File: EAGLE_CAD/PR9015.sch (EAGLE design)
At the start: 73 parts, among them J1 M3_SCREW_POST, SW1 C&K_PTS645

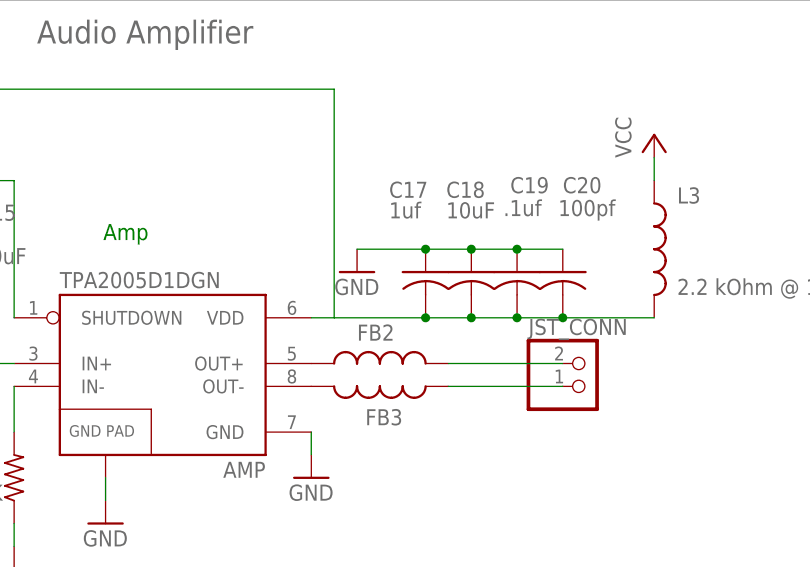
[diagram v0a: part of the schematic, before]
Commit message: okay, now we're good i think
copied R_US over to PR_Parts_Library. Then added a new package variant
and connected it with my c0402 package (created from Chris’s email).
Then went into the .brd and replaced C17 with my new part. Seems to
work.
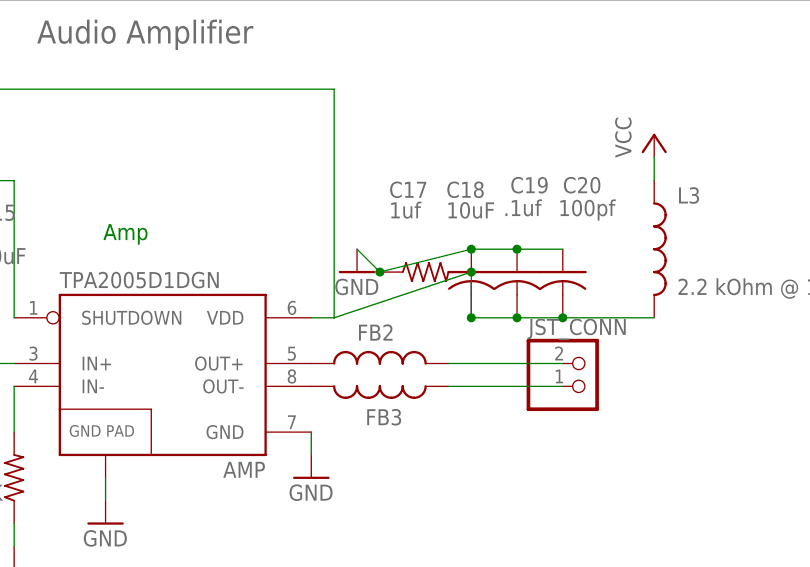
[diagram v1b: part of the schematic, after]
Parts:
- C17: device resistor:C-USC0402 -> PR_Parts_Library:R-US_
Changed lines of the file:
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@@
 <?xml version="1.0" encoding="utf-8"?>
 <!DOCTYPE eagle SYSTEM "eagle.dtd">
-<eagle version="7.2.0">
+<eagle version="6.6.0">
 <drawing>
 <settings>
@@
 <part name="C14" library="resistor" deviceset="C-US" device="C0603" value="10uF"/>
 <part name="C15" library="resistor" deviceset="C-US" device="C0603" value="10uF"/>
-<part name="C17" library="resistor" deviceset="C-US" device="C0402" value="1uf"/>
+<part name="C17" library="PR_Parts_Library" deviceset="R-US_" device="" value="1uf"/>
 <part name="C9" library="resistor" deviceset="C-US" device="C0402" value="1uF"/>
 <part name="FET2" library="PR_Parts_Library" deviceset="AO3435" device=""/>
@@
 <pinref part="C18" gate="G$1" pin="1"/>
 <junction x="208.28" y="53.34"/>
-<wire x1="208.28" y1="53.34" x2="203.2" y2="53.34" width="0.1524" layer="91"/>
+<wire x1="208.28" y1="53.34" x2="198.12" y2="50.8" width="0.1524" layer="91"/>
 <pinref part="C17" gate="G$1" pin="1"/>
-<wire x1="203.2" y1="53.34" x2="195.58" y2="53.34" width="0.1524" layer="91"/>
-<junction x="203.2" y="53.34"/>
+<wire x1="198.12" y1="50.8" x2="195.58" y2="53.34" width="0.1524" layer="91"/>
+<junction x="198.12" y="50.8"/>
 </segment>
 <segment>
@@
 <wire x1="190.5" y1="45.72" x2="193.04" y2="45.72" width="0.1524" layer="91"/>
 <pinref part="L3" gate="G$1" pin="2"/>
-<wire x1="193.04" y1="45.72" x2="203.2" y2="45.72" width="0.1524" layer="91"/>
-<wire x1="203.2" y1="45.72" x2="208.28" y2="45.72" width="0.1524" layer="91"/>
+<wire x1="193.04" y1="45.72" x2="208.28" y2="50.8" width="0.1524" layer="91"/>
+<wire x1="208.28" y1="50.8" x2="208.28" y2="45.72" width="0.1524" layer="91"/>
 <wire x1="208.28" y1="45.72" x2="213.36" y2="45.72" width="0.1524" layer="91"/>
 <wire x1="213.36" y1="45.72" x2="218.44" y2="45.72" width="0.1524" layer="91"/>
@@
 <junction x="208.28" y="45.72"/>
 <pinref part="C17" gate="G$1" pin="2"/>
-<junction x="203.2" y="45.72"/>
-</segment>
-</net>
+<junction x="208.28" y="50.8"/>
+</segment>
+</net>

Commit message: Revert cea9e40..4e97d22
This rolls back to commit cea9e40d509ff5bb8dd7e4369702d55ec1f1bc0f.
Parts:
- C17: device PR_Parts_Library:R-US_ -> resistor:C-USC0402
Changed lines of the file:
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@@
 <?xml version="1.0" encoding="utf-8"?>
 <!DOCTYPE eagle SYSTEM "eagle.dtd">
-<eagle version="6.6.0">
+<eagle version="7.2.0">
 <drawing>
 <settings>
@@
 <part name="C14" library="resistor" deviceset="C-US" device="C0603" value="10uF"/>
 <part name="C15" library="resistor" deviceset="C-US" device="C0603" value="10uF"/>
-<part name="C17" library="PR_Parts_Library" deviceset="R-US_" device="" value="1uf"/>
+<part name="C17" library="resistor" deviceset="C-US" device="C0402" value="1uf"/>
 <part name="C9" library="resistor" deviceset="C-US" device="C0402" value="1uF"/>
 <part name="FET2" library="PR_Parts_Library" deviceset="AO3435" device=""/>
@@
 <pinref part="C18" gate="G$1" pin="1"/>
 <junction x="208.28" y="53.34"/>
-<wire x1="208.28" y1="53.34" x2="198.12" y2="50.8" width="0.1524" layer="91"/>
+<wire x1="208.28" y1="53.34" x2="203.2" y2="53.34" width="0.1524" layer="91"/>
 <pinref part="C17" gate="G$1" pin="1"/>
-<wire x1="198.12" y1="50.8" x2="195.58" y2="53.34" width="0.1524" layer="91"/>
-<junction x="198.12" y="50.8"/>
+<wire x1="203.2" y1="53.34" x2="195.58" y2="53.34" width="0.1524" layer="91"/>
+<junction x="203.2" y="53.34"/>
 </segment>
 <segment>
@@
 <wire x1="190.5" y1="45.72" x2="193.04" y2="45.72" width="0.1524" layer="91"/>
 <pinref part="L3" gate="G$1" pin="2"/>
-<wire x1="193.04" y1="45.72" x2="208.28" y2="50.8" width="0.1524" layer="91"/>
-<wire x1="208.28" y1="50.8" x2="208.28" y2="45.72" width="0.1524" layer="91"/>
+<wire x1="193.04" y1="45.72" x2="203.2" y2="45.72" width="0.1524" layer="91"/>
+<wire x1="203.2" y1="45.72" x2="208.28" y2="45.72" width="0.1524" layer="91"/>
 <wire x1="208.28" y1="45.72" x2="213.36" y2="45.72" width="0.1524" layer="91"/>
 <wire x1="213.36" y1="45.72" x2="218.44" y2="45.72" width="0.1524" layer="91"/>
@@
 <junction x="208.28" y="45.72"/>
 <pinref part="C17" gate="G$1" pin="2"/>
-<junction x="208.28" y="50.8"/>
-</segment>
-</net>
+<junction x="203.2" y="45.72"/>
+</segment>
+</net>

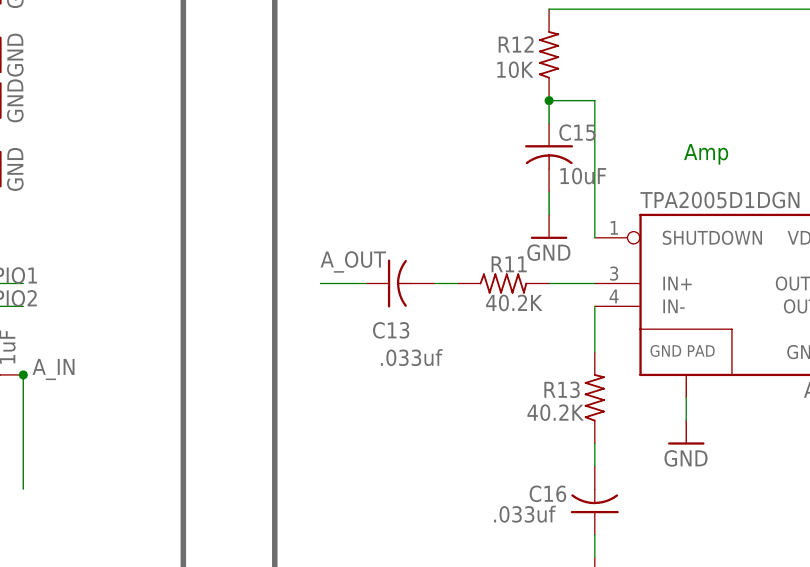
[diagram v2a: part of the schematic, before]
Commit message: more c0402 changes
and i swapped out c13 and it works
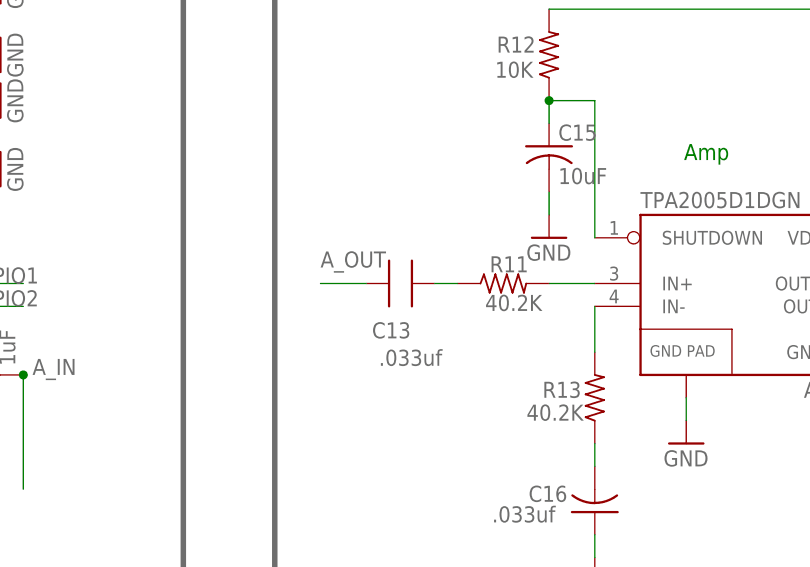
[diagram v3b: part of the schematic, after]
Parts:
- C13: device resistor:C-USC0402 -> PR_Parts_Library:CAP_SMT
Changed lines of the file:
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@@
 <?xml version="1.0" encoding="utf-8"?>
 <!DOCTYPE eagle SYSTEM "eagle.dtd">
-<eagle version="7.2.0">
+<eagle version="6.6.0">
 <drawing>
 <settings>
@@
 <part name="R11" library="resistor" deviceset="R-US_" device="R0402" value="40.2K"/>
 <part name="R13" library="resistor" deviceset="R-US_" device="R0402" value="40.2K"/>
-<part name="C13" library="resistor" deviceset="C-US" device="C0402" value=".033uf"/>
+<part name="C13" library="PR_Parts_Library" deviceset="CAP_SMT" device="" value=".033uf"/>
 <part name="C16" library="resistor" deviceset="C-US" device="C0402" value=".033uf"/>
 <part name="GND26" library="SparkFun-Aesthetics" deviceset="GND" device=""/>

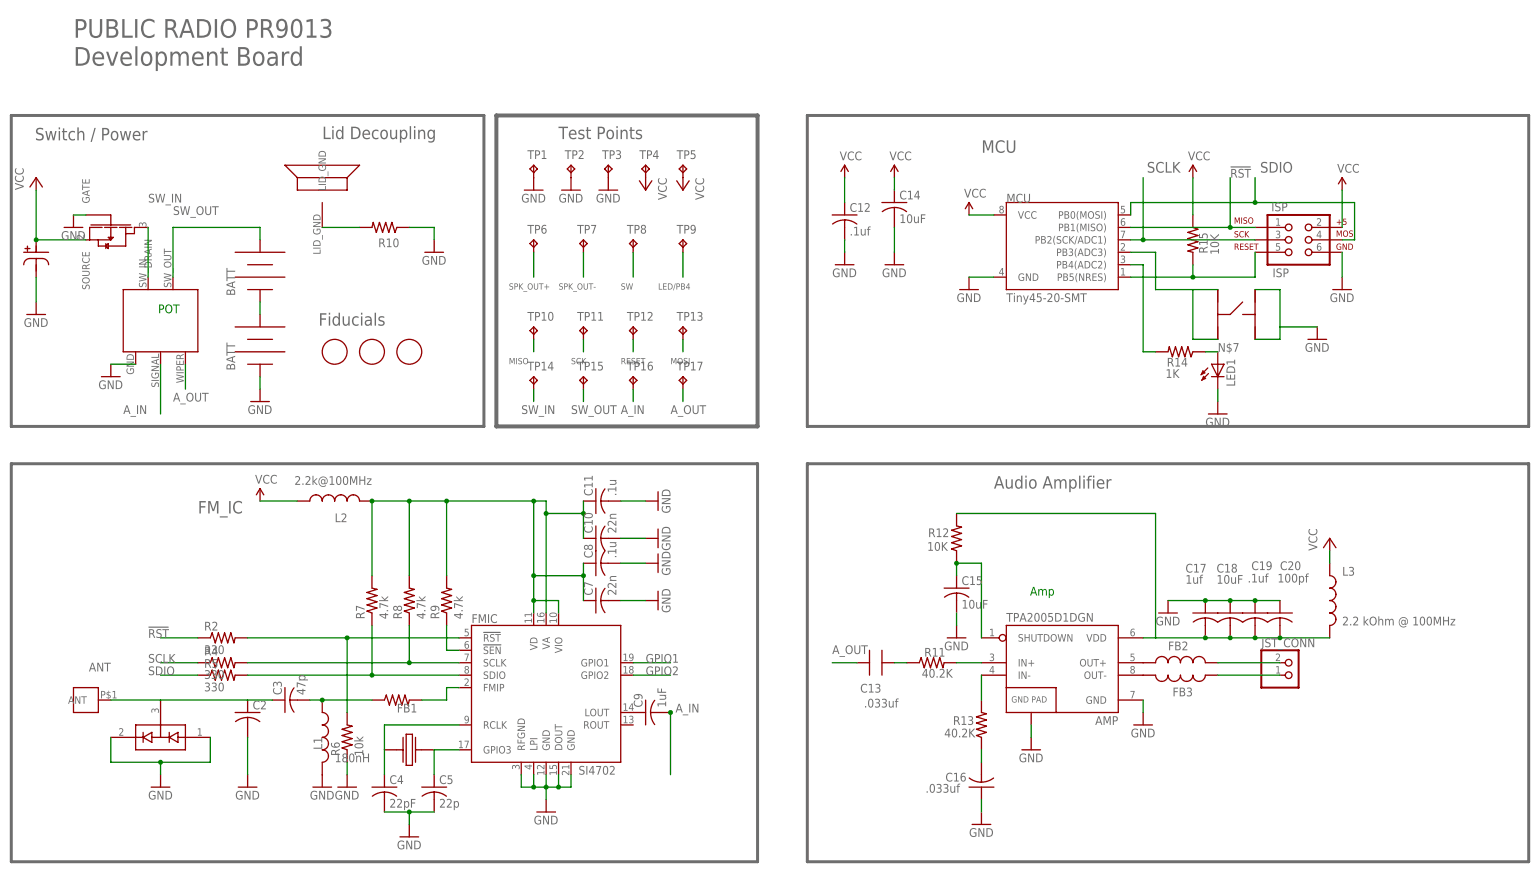
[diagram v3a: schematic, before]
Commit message: Updated Layout / SCH
Increased font size and width ratio, made them vectors
Changed all 0402 caps to 0402 for Worthington’s Specs
Straightened all 0402 traces on caps
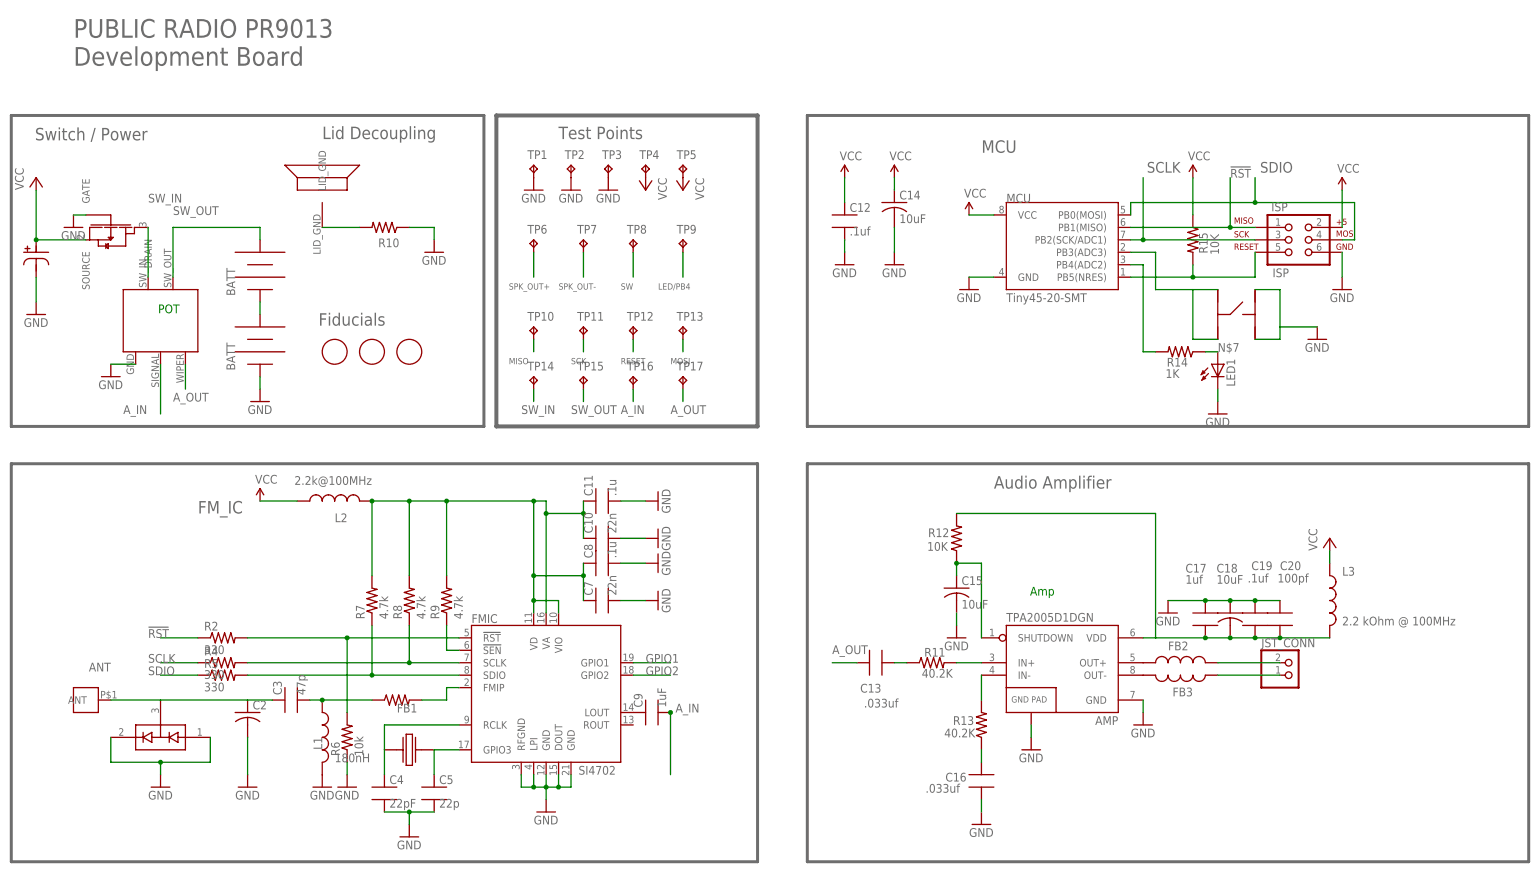
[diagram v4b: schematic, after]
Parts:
- C10, C11, C12, C16, C17, C19, C20, C3, C4, C5, C7, C8, C9: device resistor:C-USC0402 -> PR_Parts_Library:CAP_SMT
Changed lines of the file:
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@@
 <part name="R13" library="resistor" deviceset="R-US_" device="R0402" value="40.2K"/>
 <part name="C13" library="PR_Parts_Library" deviceset="CAP_SMT" device="" value=".033uf"/>
-<part name="C16" library="resistor" deviceset="C-US" device="C0402" value=".033uf"/>
+<part name="C16" library="PR_Parts_Library" deviceset="CAP_SMT" device="" value=".033uf"/>
 <part name="GND26" library="SparkFun-Aesthetics" deviceset="GND" device=""/>
 <part name="GND28" library="SparkFun-Aesthetics" deviceset="GND" device=""/>
@@
 <part name="GND21" library="SparkFun" deviceset="GND" device=""/>
 <part name="GND16" library="SparkFun" deviceset="GND" device=""/>
-<part name="C12" library="resistor" deviceset="C-US" device="C0402" value=".1uf"/>
-<part name="C19" library="resistor" deviceset="C-US" device="C0402" value=".1uf"/>
-<part name="C20" library="resistor" deviceset="C-US" device="C0402" value="100pf"/>
+<part name="C12" library="PR_Parts_Library" deviceset="CAP_SMT" device="" value=".1uf"/>
+<part name="C19" library="PR_Parts_Library" deviceset="CAP_SMT" device="" value=".1uf"/>
+<part name="C20" library="PR_Parts_Library" deviceset="CAP_SMT" device="" value="100pf"/>
 <part name="R10" library="resistor" deviceset="R-US_" device="R0805"/>
 <part name="D1" library="SparkFun-DiscreteSemi" deviceset="BAV99" device=""/>
@@
 <part name="JST_CONN" library="adafruit" deviceset="JST_2PIN" device="-SMT-RA"/>
 <part name="C2" library="resistor" deviceset="C-US" device="C0402"/>
-<part name="C3" library="resistor" deviceset="C-US" device="C0402" value="47p"/>
-<part name="C4" library="resistor" deviceset="C-US" device="C0402" value="22pF"/>
-<part name="C5" library="resistor" deviceset="C-US" device="C0402" value="22p"/>
-<part name="C7" library="resistor" deviceset="C-US" device="C0402" value="22n"/>
-<part name="C8" library="resistor" deviceset="C-US" device="C0402" value=".1u"/>
+<part name="C3" library="PR_Parts_Library" deviceset="CAP_SMT" device="" value="47p"/>
+<part name="C4" library="PR_Parts_Library" deviceset="CAP_SMT" device="" value="22pF"/>
+<part name="C5" library="PR_Parts_Library" deviceset="CAP_SMT" device="" value="22p"/>
+<part name="C7" library="PR_Parts_Library" deviceset="CAP_SMT" device="" value="22n"/>
+<part name="C8" library="PR_Parts_Library" deviceset="CAP_SMT" device="" value=".1u"/>
 <part name="R2" library="resistor" deviceset="R-US_" device="R0402" value="330"/>
 <part name="R4" library="resistor" deviceset="R-US_" device="R0402" value="330"/>
@@
 <part name="R7" library="resistor" deviceset="R-US_" device="R0402" value="4.7k"/>
 <part name="R6" library="resistor" deviceset="R-US_" device="R0402" value="10k"/>
-<part name="C10" library="resistor" deviceset="C-US" device="C0402" value="22n"/>
-<part name="C11" library="resistor" deviceset="C-US" device="C0402" value=".1u"/>
+<part name="C10" library="PR_Parts_Library" deviceset="CAP_SMT" device="" value="22n"/>
+<part name="C11" library="PR_Parts_Library" deviceset="CAP_SMT" device="" value=".1u"/>
 <part name="SW1" library="PR_Parts_Library" deviceset="C&amp;K_PTS645" device=""/>
 <part name="C1" library="PR_Parts_Library" deviceset="NICHICON_SERIESUD" device="" value="220uF"/>
@@
 <part name="C14" library="resistor" deviceset="C-US" device="C0603" value="10uF"/>
 <part name="C15" library="resistor" deviceset="C-US" device="C0603" value="10uF"/>
-<part name="C17" library="resistor" deviceset="C-US" device="C0402" value="1uf"/>
-<part name="C9" library="resistor" deviceset="C-US" device="C0402" value="1uF"/>
+<part name="C17" library="PR_Parts_Library" deviceset="CAP_SMT" device="" value="1uf"/>
+<part name="C9" library="PR_Parts_Library" deviceset="CAP_SMT" device="" value="1uF"/>
 <part name="FET2" library="PR_Parts_Library" deviceset="AO3435" device=""/>
 <part name="U$1" library="PR_Parts_Library" deviceset="CE32A_FOR_JST" device=""/>
